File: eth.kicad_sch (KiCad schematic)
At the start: 1 part, among them J3 RJ45_Abracon_ARJM11B1-502-AB-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

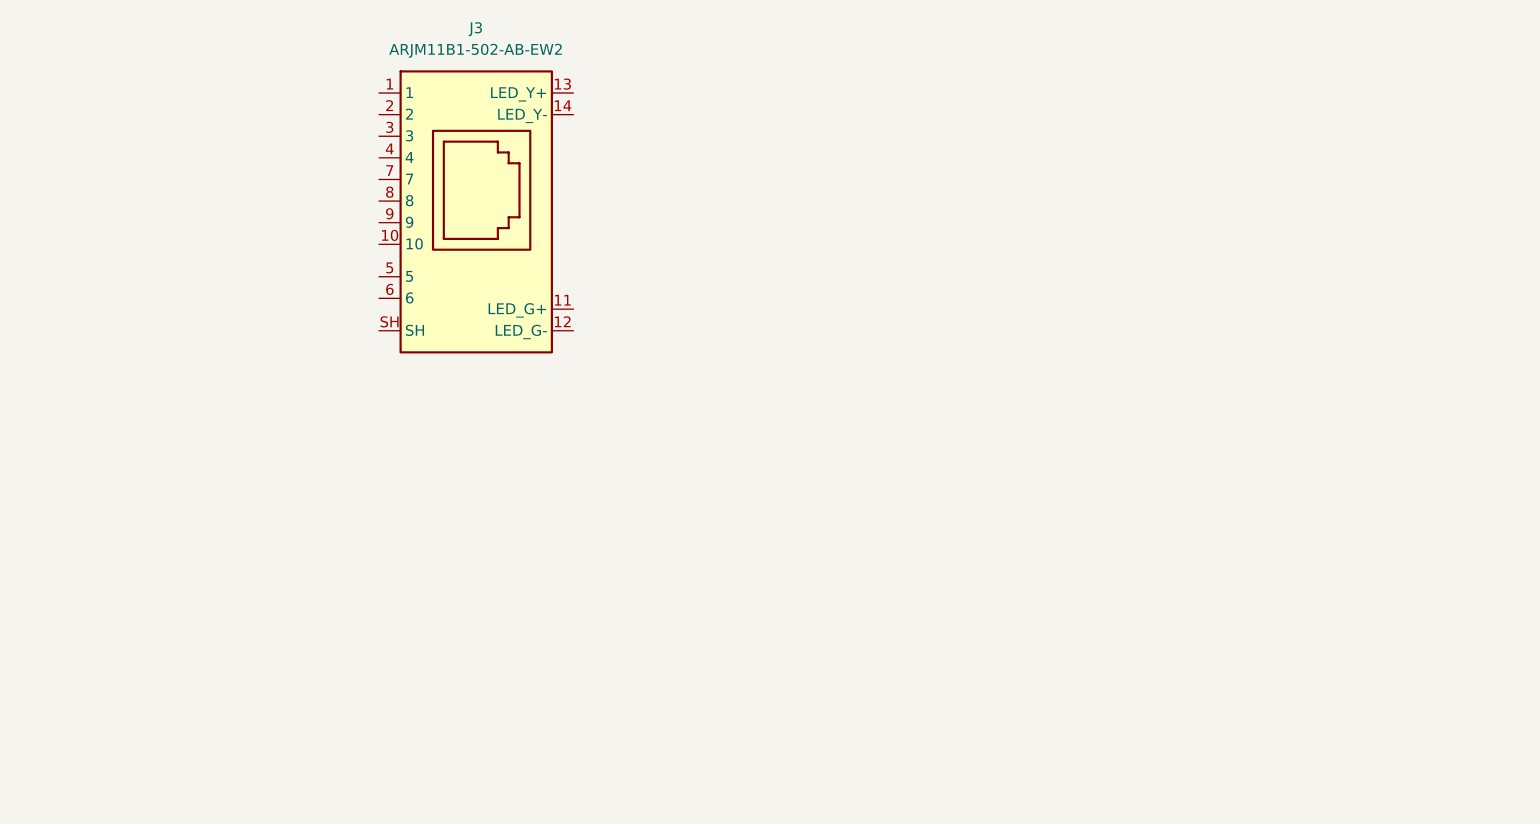
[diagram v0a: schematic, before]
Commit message: [#94684] Add ports to subsheets
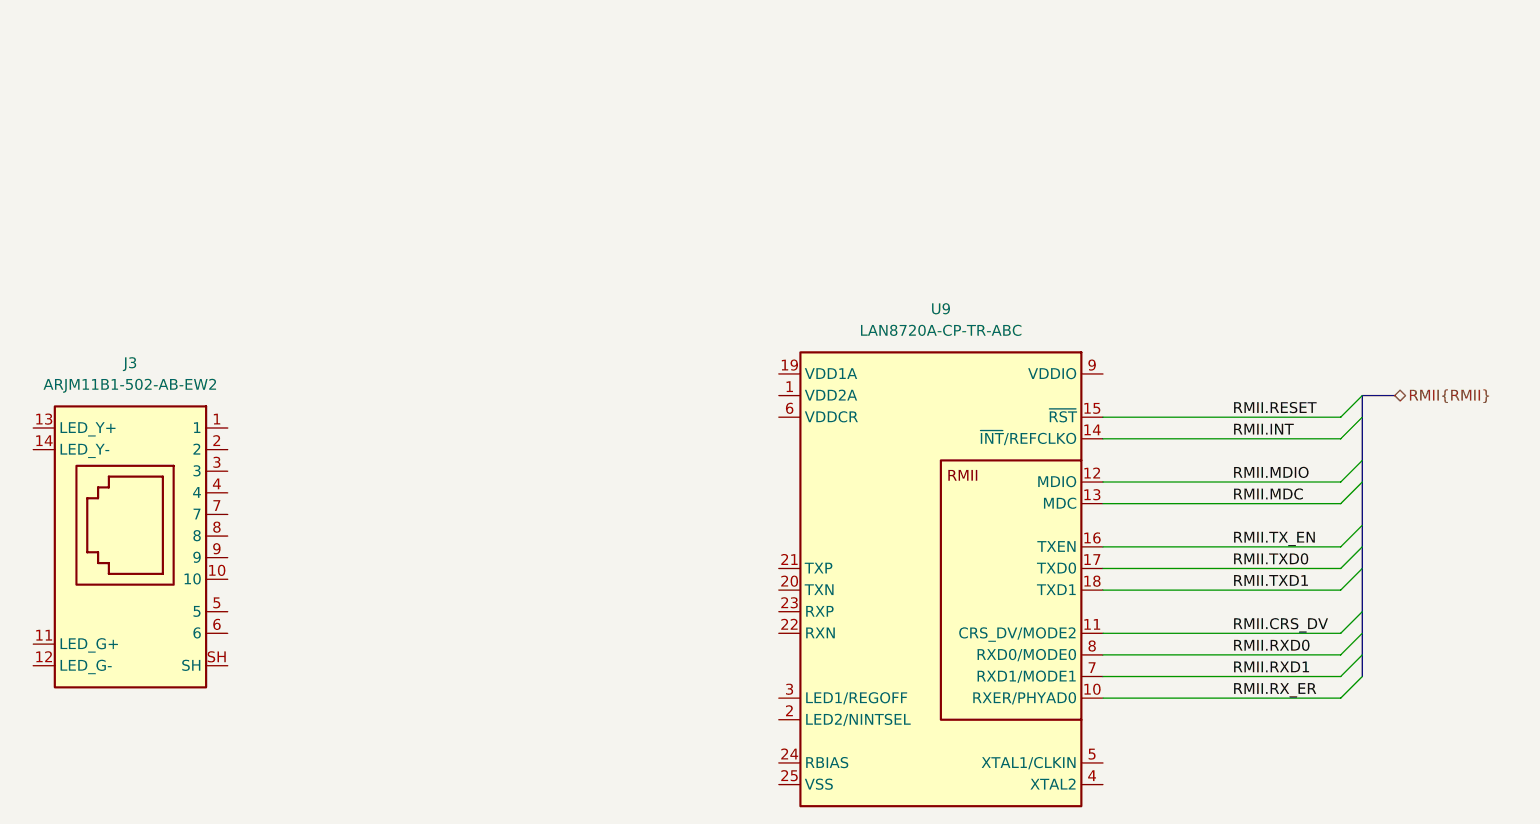
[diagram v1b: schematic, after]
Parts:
- added U9: LAN8720A-CP-TR-ABC, antmicro-footprints:QFN-24-1EP_4x4mm_P0.5mm_EP2.6x2.6mm, symbol antmicroInterfaceControllers:LAN8720A-CP-TR-ABC
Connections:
- new net RMII.CRS_DV: U9.11 (CRS_DV/MODE2)
- new net RMII.INT: U9.14 (~{INT}/REFCLKO)
- new net RMII.MDC: U9.13 (MDC)
- new net RMII.MDIO: U9.12 (MDIO)
- new net RMII.RESET: U9.15 (~{RST})
- new net RMII.RXD0: U9.8 (RXD0/MODE0)
- new net RMII.RXD1: U9.7 (RXD1/MODE1)
- new net RMII.RX_ER: U9.10 (RXER/PHYAD0)
- new net RMII.TXD0: U9.17 (TXD0)
- new net RMII.TXD1: U9.18 (TXD1)
- new net RMII.TX_EN: U9.16 (TXEN)
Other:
- moved on the sheet: J3

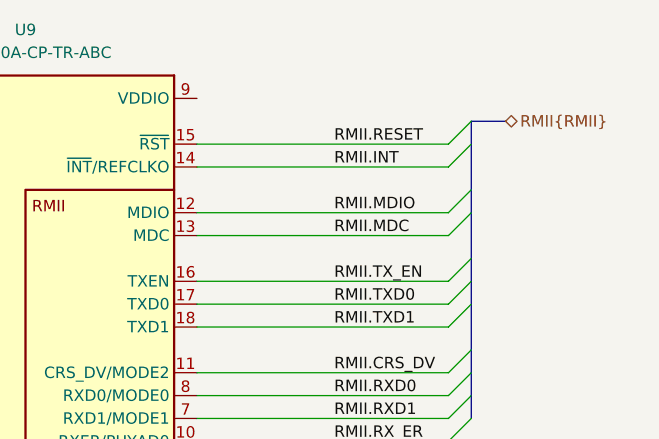
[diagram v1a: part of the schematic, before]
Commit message: [#94727] Add RMII, IOs, JTAG, UART, QSPI connection to MCU
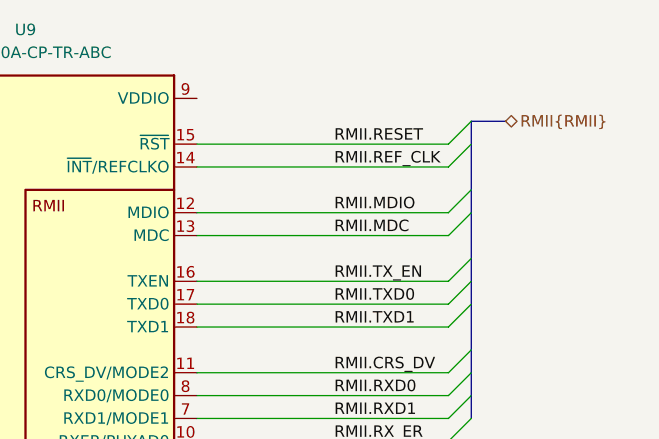
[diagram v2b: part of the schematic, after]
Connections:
- net RMII.INT renamed RMII.REF_CLK
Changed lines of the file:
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@@
+	)
+	(bus_entry
+		(at 259.08 114.3)
+		(size -2.54 2.54)
+		(stroke
+			(width 0)
+			(type default)
+		)
 	)
 	(bus_entry
@@
 	)
 	(bus_entry
-		(at 259.08 114.3)
-		(size -2.54 2.54)
-		(stroke
-			(width 0)
-			(type default)
-		)
-	)
-	(bus_entry
 		(at 259.08 132.08)
 		(size -2.54 2.54)
@@
 	(bus
 		(pts
-			(xy 259.08 114.3) (xy 259.08 111.76)
-		)
-		(stroke
-			(width 0)
-			(type default)
-		)
-	)
-	(bus
-		(pts
-			(xy 259.08 119.38) (xy 259.08 114.3)
+			(xy 259.08 111.76) (xy 259.08 114.3)
+		)
+		(stroke
+			(width 0)
+			(type default)
+		)
+	)
+	(wire
+		(pts
+			(xy 228.6 116.84) (xy 256.54 116.84)
 		)
 		(stroke
@@
 		)
 	)
+	(bus
+		(pts
+			(xy 259.08 114.3) (xy 259.08 119.38)
+		)
+		(stroke
+			(width 0)
+			(type default)
+		)
+	)
 	(wire
 		(pts
@@
 		(pts
 			(xy 259.08 137.16) (xy 259.08 139.7)
-		)
-		(stroke
-			(width 0)
-			(type default)
-		)
-	)
-	(wire
-		(pts
-			(xy 228.6 116.84) (xy 256.54 116.84)
 		)
 		(stroke
@@
 		)
 	)
+	(label "RMII.REF_CLK"
+		(at 243.84 116.84 0)
+		(effects
+			(font
+				(size 1.27 1.27)
+			)
+			(justify left bottom)
+		)
+	)
 	(label "RMII.RESET"
 		(at 243.84 114.3 0)
 		(effects
 			(font
-				(size 1.27 1.27)
-			)
-			(justify left bottom)
-		)
-	)
-	(label "RMII.INT"
-		(at 243.84 116.84 0)
-		(effects
-			(font

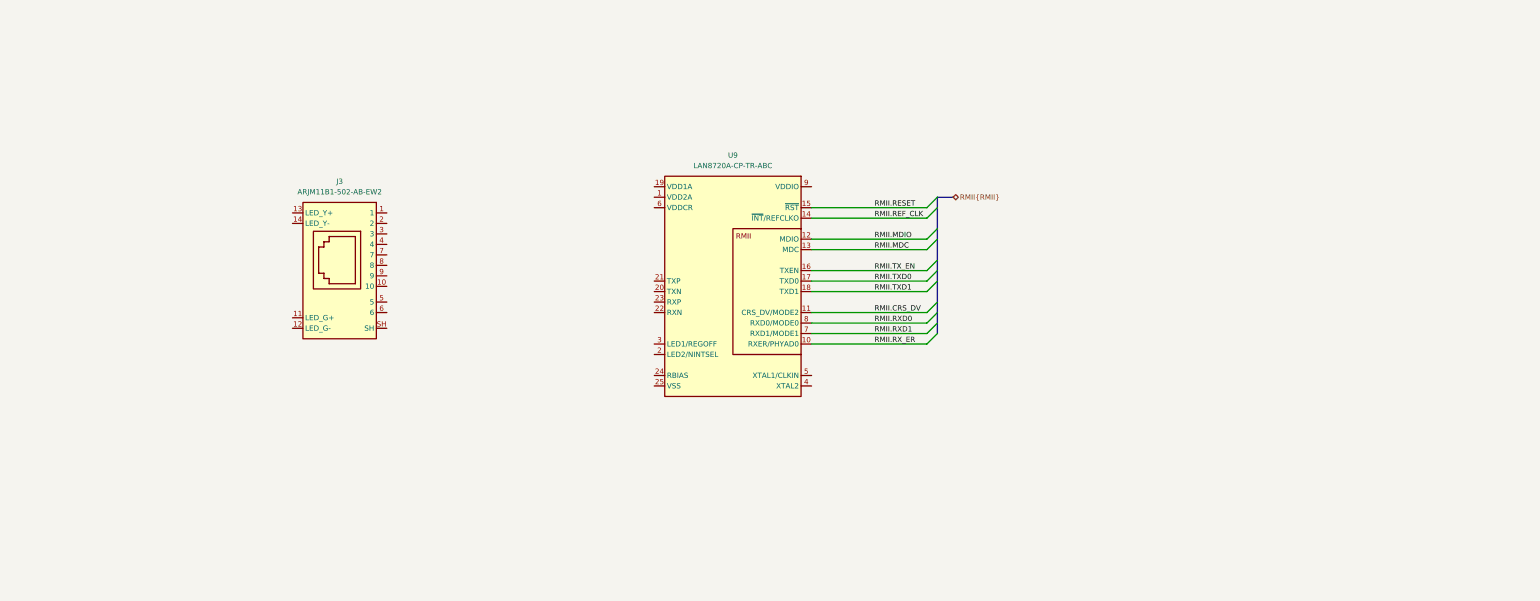
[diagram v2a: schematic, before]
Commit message: [#94823] Add ethernet implementation
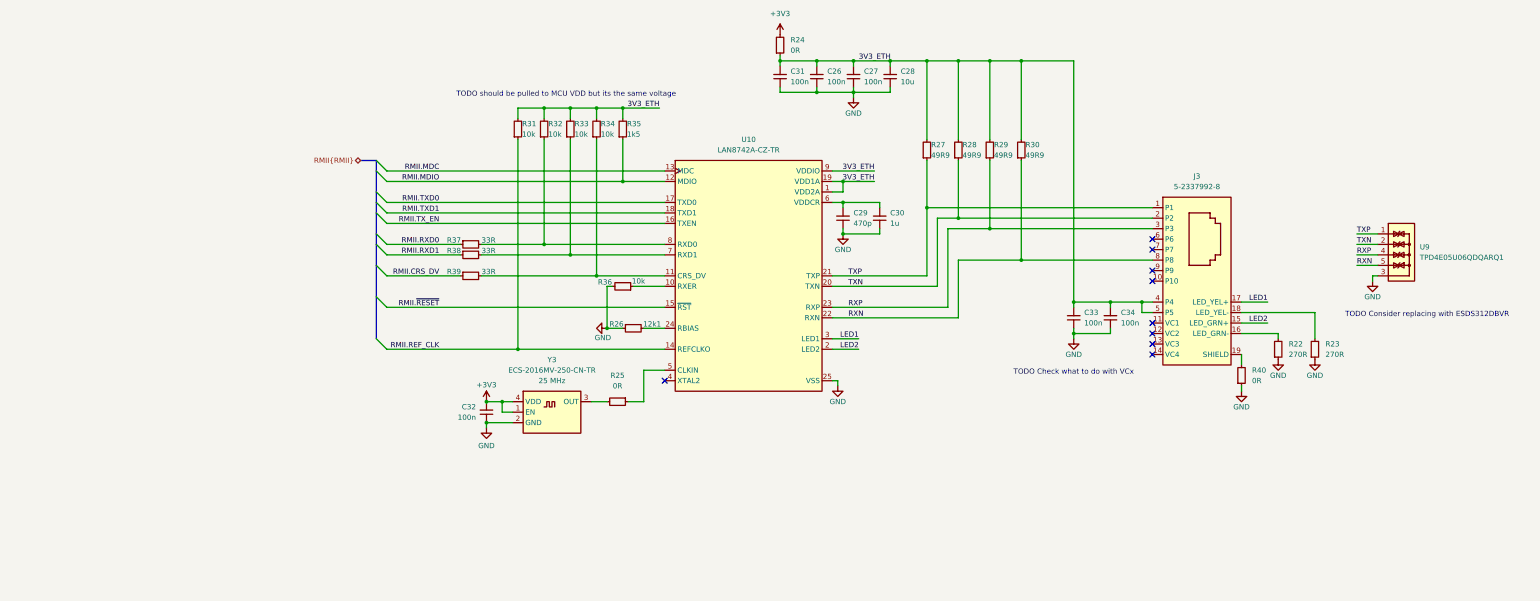
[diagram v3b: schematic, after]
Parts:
- removed J3: RJ45_Abracon_ARJM11B1-502-AB-EW2, antmicro-footprints:RJ45_ARJM11B1-502-AB-EW2_Horizontal, symbol antmicroModularConnectorsJacks:RJ45_Abracon_ARJM11B1-502-AB-EW2
- removed U9: LAN8720A-CP-TR-ABC, antmicro-footprints:QFN-24-1EP_4x4mm_P0.5mm_EP2.6x2.6mm, symbol antmicroInterfaceControllers:LAN8720A-CP-TR-ABC
- added C26, C27, C31, C32, C33, C34: C_100n_0402, antmicro-footprints:C_0402_1005Metric, symbol antmicroCapacitors0402:C_100n_0402
- added C28: C_10u_0402, antmicro-footprints:C_0402_1005Metric, symbol antmicroCapacitors0402:C_10u_0402
- added C29: C_470p_0402, antmicro-footprints:C_0402_1005Metric, symbol antmicroCapacitors0402:C_470p_0402
- added C30: C_1u_0402, antmicro-footprints:C_0402_1005Metric, symbol antmicroCapacitors0402:C_1u_0402
- added J3: Bus_RJ45_5-2337992-8, antmicro-footprints:RJ45_X-2337992-8_Horizontal, symbol antmicroModularConnectorsJacksWithMagnetics:Bus_RJ45_5-2337992-8
- added R22, R23: R_270R_0402, antmicro-footprints:R_0402_1005Metric, symbol antmicroResistors0402:R_270R_0402
- added R24, R25, R40: R_0R_0402, antmicro-footprints:R_0402_1005Metric, symbol antmicroResistors0402:R_0R_0402
- added R26: R_12k1_0402, antmicro-footprints:R_0402_1005Metric, symbol antmicroResistors0402:R_12k1_0402
- added R27, R28, R29, R30: R_49R9_0402, antmicro-footprints:R_0402_1005Metric, symbol antmicroResistors0402:R_49R9_0402
- added R31, R32, R33, R34, R36: R_10k_0402, antmicro-footprints:R_0402_1005Metric, symbol antmicroResistors0402:R_10k_0402
- added R35: R_1k5_0402, antmicro-footprints:R_0402_1005Metric, symbol antmicroResistors0402:R_1k5_0402
- added R37, R38, R39: R_33R_0402, antmicro-footprints:R_0402_1005Metric, symbol antmicroResistors0402:R_33R_0402
- added U10: LAN8742A-CZ-TR, antmicro-footprints:VQFN-24-1EP_4x4x0.9mm_P0.5mm_EP2.6x2.6mm, symbol antmicroInterfaceControllers:LAN8742A-CZ-TR
- added U9: TPD4E05U06QDQARQ1, antmicro-footprints:USON-10_2.5x1mm_P0.5mm, symbol antmicroTVSDiodes:TPD4E05U06QDQARQ1
- added Y3: Oscillator_25MHz_ESC_2016MV, antmicro-footprints:Oscillator_SMD_ECS_2016MV_2x1.6x0.85mm, symbol antmicroOscillators:Oscillator_25MHz_ESC_2016MV
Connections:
- net RMII.CRS_DV: now also R39.1
- net RMII.MDC: now also U10.13 (MDC)
- net RMII.MDIO: now also R35.1, U10.12 (MDIO)
- net RMII.REF_CLK: now also R31.1, U10.14 (~{INT})
- net RMII.RXD0: now also R37.1
- net RMII.RXD1: now also R38.1
- net RMII.TXD0: now also U10.17 (TXD0)
- net RMII.TXD1: now also U10.18 (TXD1)
- net RMII.TX_EN: now also U10.16 (TXEN)
- new net: R33.1, R38.2, U10.7 (RXD1)
- new net: C29.2, C30.2, U10.6 (VDDCR)
- new net: R36.1, U10.10 (RXER)
- new net: R34.1, R39.2, U10.11 (CRS_DV)
- new net: J3.18 (LED_YEL-), R23.2
- new net: R25.2, Y3.3 (OUT)
- new net: J3.16 (LED_GRN-), R22.2
- new net: J3.19 (SHIELD), J3.20 (SHIELD), R40.2
- new net: R26.2, U10.24 (RBIAS)
- new net: R32.1, R37.2, U10.8 (RXD0)
- new net: R25.1, U10.5 (XTAL1)
- new net +3V3: C32.2, R24.2, Y3.1 (EN), Y3.4 (VDD)
- new net 3V3_ETH: C26.2, C27.2, C28.2, C31.2, C33.2, C34.2, J3.4 (P4), J3.5 (P5), R24.1, R27.2, R28.2, R29.2, R30.2, R31.2, R32.2, R33.2, R34.2, R35.2, U10.1 (VDD2A), U10.19 (VDD1A), U10.9 (VDDIO)
- new net GND: C26.1, C27.1, C28.1, C29.1, C30.1, C31.1, C32.1, C33.1, C34.1, R22.1, R23.1, R26.1, R36.2, R40.1, U10.25 (VSS), U9.3, U9.8, Y3.2 (GND)
- new net LED1: J3.17 (LED_YEL+), U10.3 (LED1)
- new net LED2: J3.15 (LED_GRN+), U10.2 (LED2)
- new net RMII.~{RESET}: U10.15 (~{RST})
- new net RXN: J3.8 (P8), R30.1, U10.22 (RXN), U9.5, U9.6
- new net RXP: J3.3 (P3), R29.1, U10.23 (RXP), U9.4, U9.7
- new net TXN: J3.2 (P2), R28.1, U10.20 (TXN), U9.2, U9.9
- new net TXP: J3.1 (P1), R27.1, U10.21 (TXP), U9.1, U9.10
- no-connect marks 0 -> 9
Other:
- note added: "TODO Check what to do with VCx"
- note added: "TODO Consider replacing with ESDS312DBVR"
- note added: "TODO should be pulled to MCU VDD but its the same voltage"

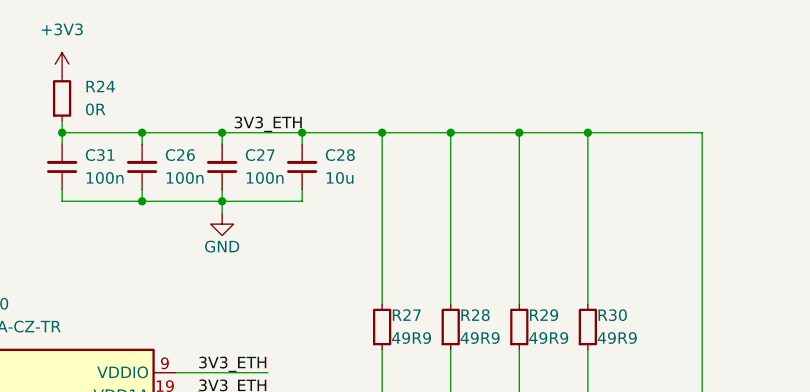
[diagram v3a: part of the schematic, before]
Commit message: [#95036] Solve basic ERCs
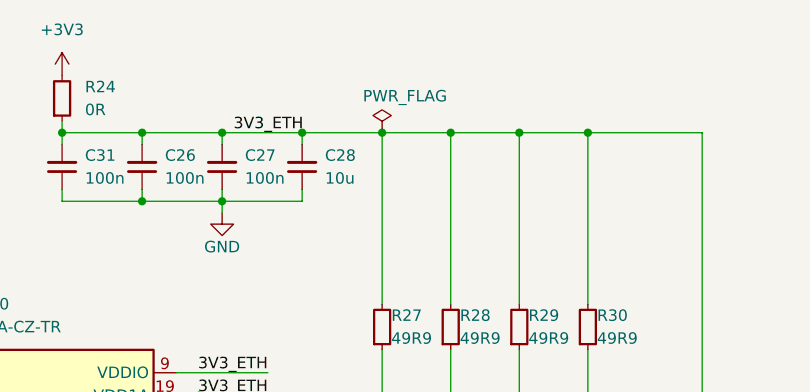
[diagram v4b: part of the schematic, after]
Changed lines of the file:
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@@
+	)
+	(symbol
+		(lib_id "antmicropower:PWR_FLAG")
+		(at 256.54 78.74 0)
+		(mirror y)
+		(unit 1)
+		(exclude_from_sim no)
+		(in_bom yes)
+		(on_board yes)
+		(dnp no)
+		(property "Reference" "#FLG09"
+			(at 256.54 76.835 0)
+			(effects
+				(font
+					(size 1.27 1.27)
+				)
+				(hide yes)
+			)
+		)
+		(property "Value" "PWR_FLAG"
+			(at 259.08 74.676 0)
+			(effects
+				(font
+					(size 1.27 1.27)
+				)
+			)
+		)
+		(property "Footprint" ""
+			(at 256.54 78.74 0)
+			(effects
+				(font
+					(size 1.27 1.27)
+				)
+				(hide yes)
+			)
+		)
+		(property "Datasheet" ""
+			(at 256.54 78.74 0)
+			(effects
+				(font
+					(size 1.27 1.27)
+				)
+				(hide yes)
+			)
+		)
+		(property "Description" ""
+			(at 256.54 81.28 0)
+			(effects
+				(font
+					(size 1.27 1.27)
+				)
+				(justify left bottom)
+				(hide yes)
+			)
+		)
+		(pin "1"
+		)
+		(instances
+			(project "renode-reference-platform"
+				(path "/126ae87b-f292-4372-94ff-ae46971d67ab/f0f01ea9-8179-4d1d-a204-7bfa46e66030"
+					(reference "#FLG09")
+					(unit 1)
+				)
+			)
+		)
 	)
 	(symbol

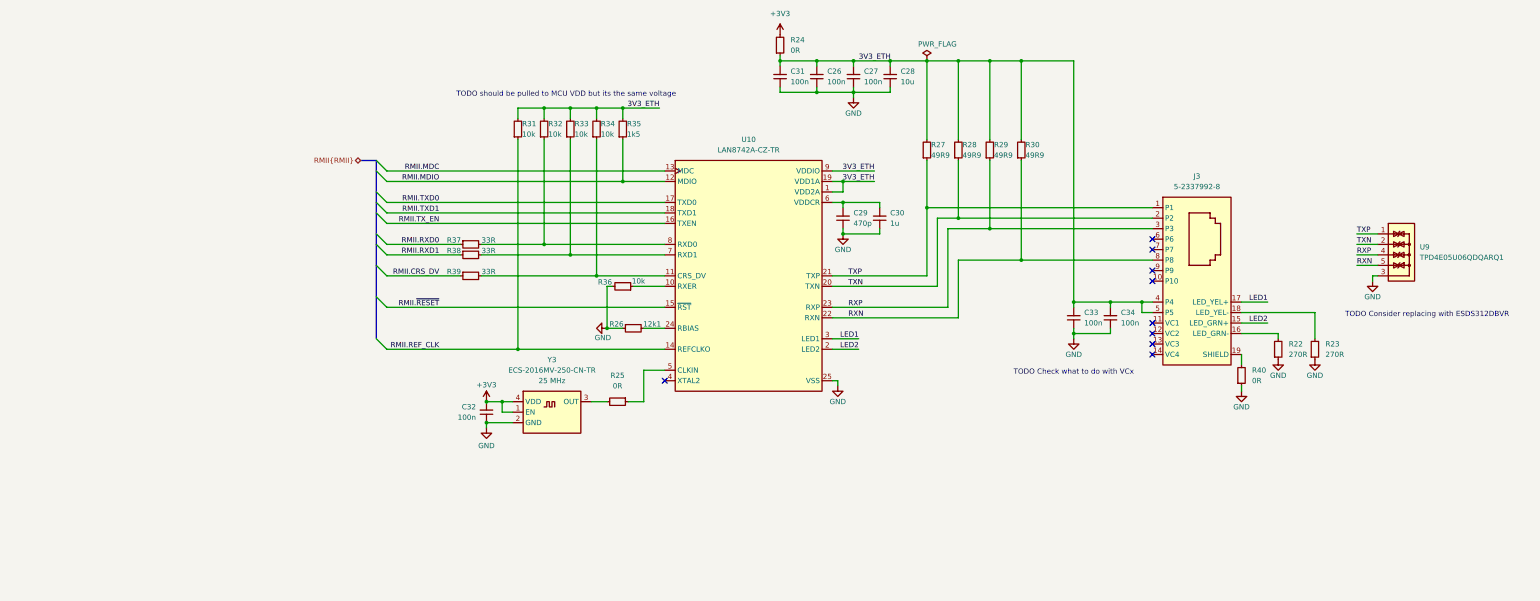
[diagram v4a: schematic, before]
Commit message: [#95036] Add schematic markings
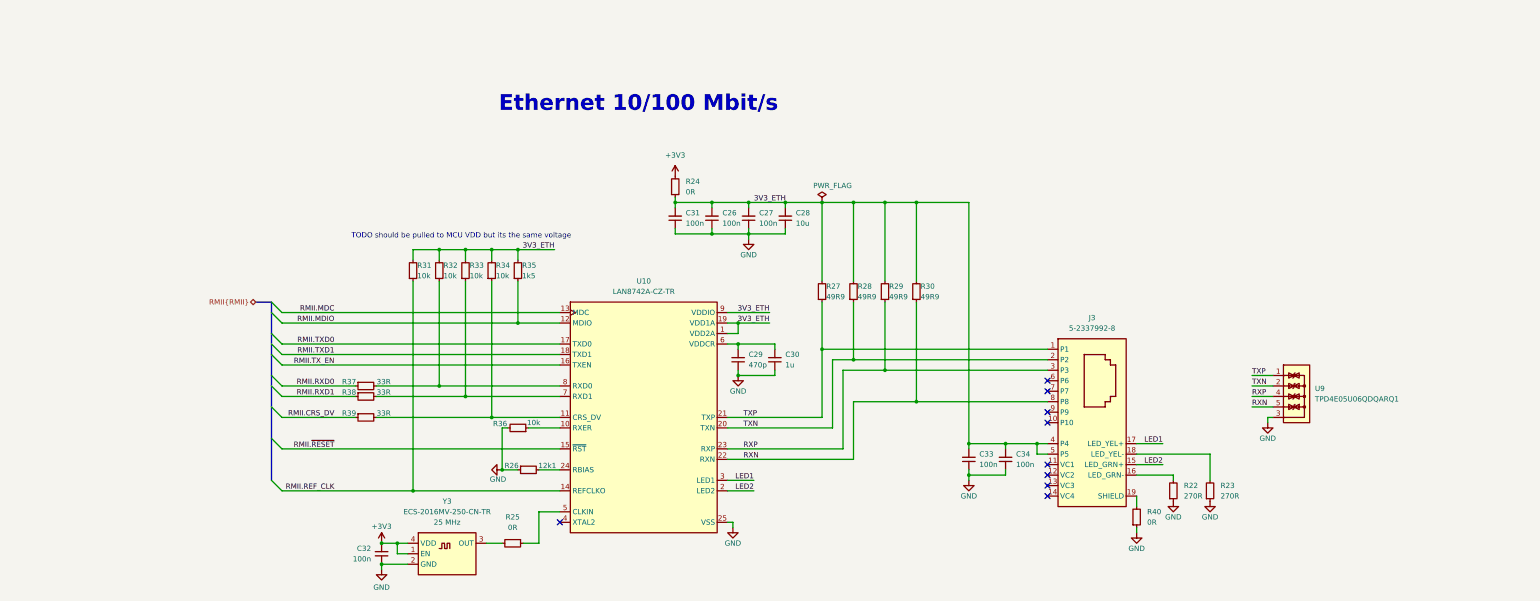
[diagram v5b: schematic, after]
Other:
- note added: "Ethernet 10/100 Mbit/s"
- note removed: "TODO Check what to do with VCx"
- note removed: "TODO Consider replacing with ESDS312DBVR"
- moved on the sheet: C26, C27, C28, C29, C30, C31, C32, C33, C34, J3, R22, R23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
